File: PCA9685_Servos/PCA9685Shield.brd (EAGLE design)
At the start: 58.2 x 36.2 mm, 13 parts, among them U1 PCA9685

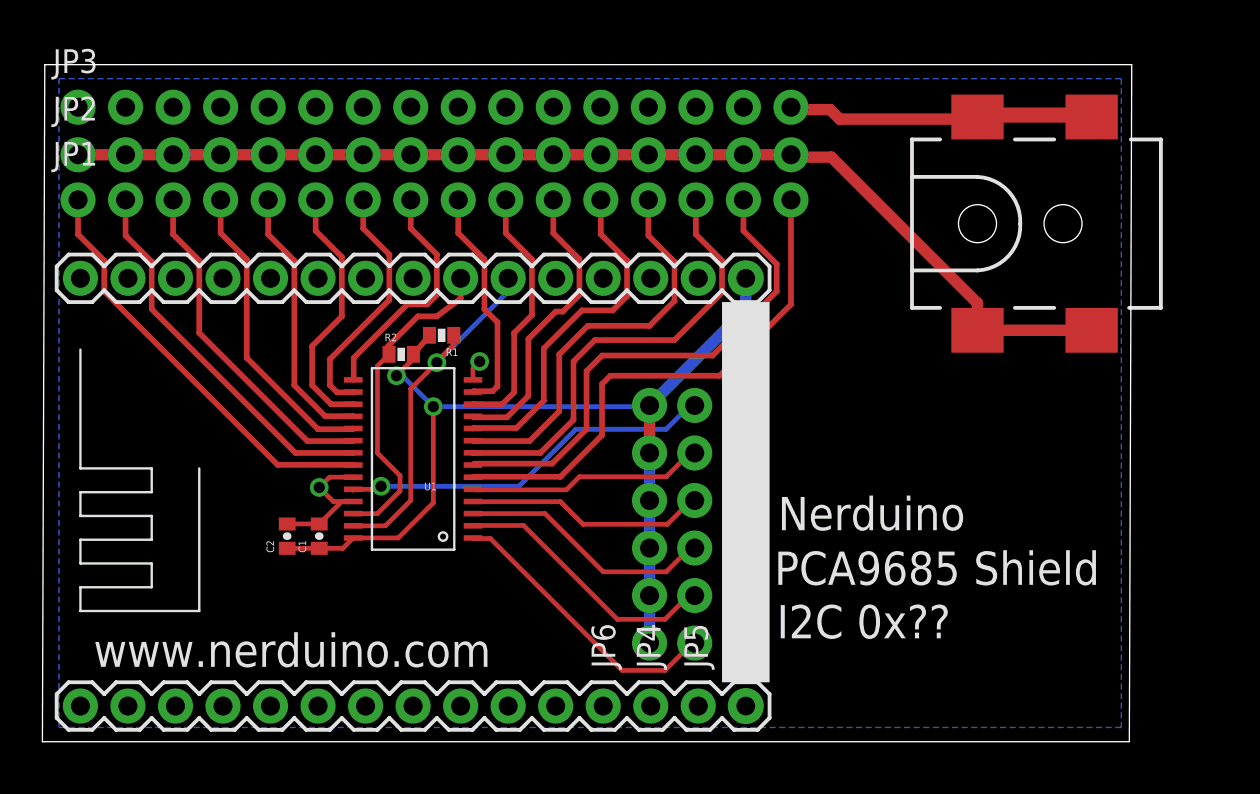
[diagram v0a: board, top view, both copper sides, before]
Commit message: Added solder jumpers for address and added resistors to output pins on pca9685 shield Updated labels
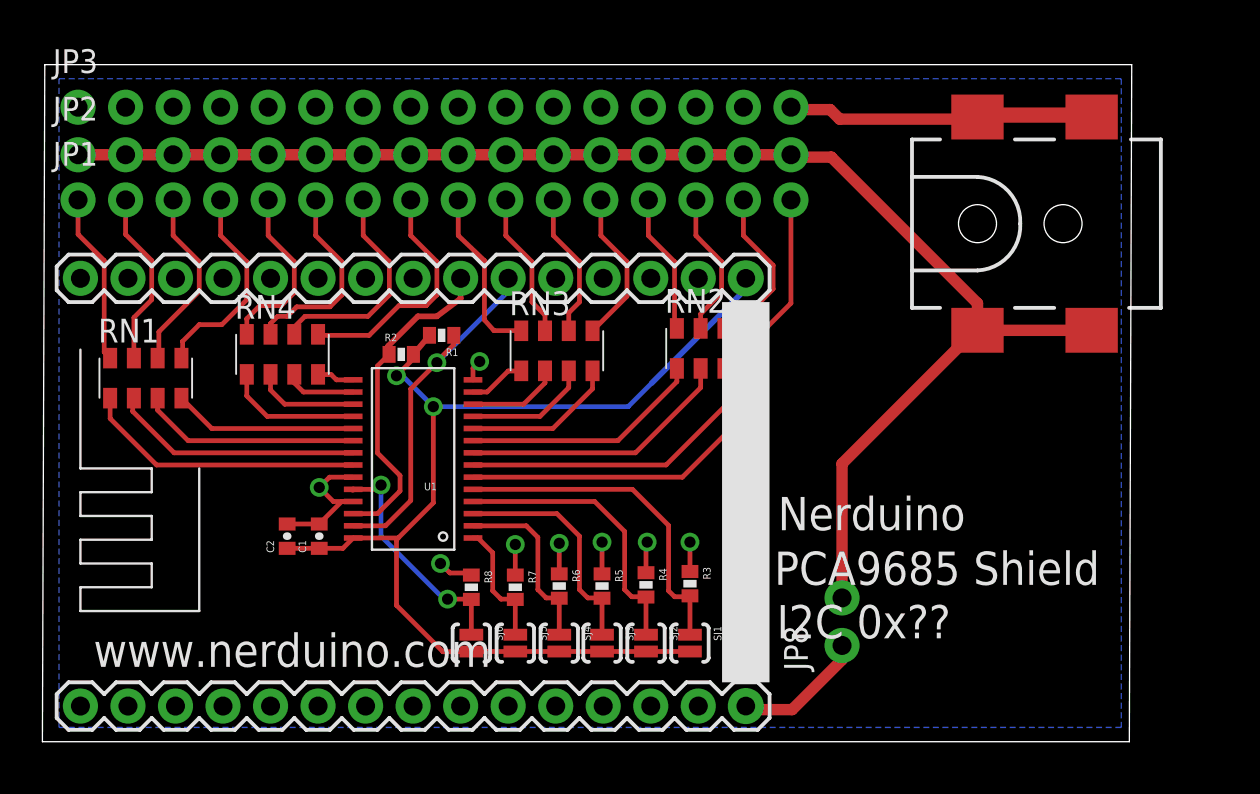
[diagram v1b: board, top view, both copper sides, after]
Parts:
- removed JP4, JP5, JP6: (no value), SparkFun-Connectors:1X06_NO_SILK
- added JP8: (no value), SparkFun:1X02_NO_SILK
- added R3, R4, R5, R6, R7, R8: 10k, SparkFun:0402-RES
- added RN1, RN2, RN3, RN4: 220, resistor-dil:EXBS8V
- added SJ1, SJ2, SJ3, SJ4, SJ5, SJ6: SOLDERJUMPERNO, SparkFun:SJ_2S-NO
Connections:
- removed net N$7: JP4.5, U1.5
- new net N$1: JP8.1, U$1.15
- new net N$27: JP1.2, RN1.7
- new net N$28: JP1.1, RN1.8
- new net N$29: RN1.3, U1.20
- new net N$30: RN1.4, U1.19
- new net N$31: RN4.1, U1.18
- new net N$32: RN4.2, U1.17
- new net N$33: RN4.3, U1.16
- new net N$34: RN4.4, U1.15
- new net N$35: RN3.1, U1.13
- new net N$36: RN3.2, U1.12
- new net N$37: RN3.3, U1.11
- new net N$38: RN3.4, U1.10
- new net N$39: RN2.1, U1.9
- new net N$40: RN2.2, U1.8
- new net N$41: RN2.3, U1.7
- new net N$42: JP1.16, RN2.5
- new net N$43: R3.2, SJ1.1, U1.5
- net 3.3V: now also SJ1.2, SJ2.2, SJ3.2, SJ4.2, SJ5.2, SJ6.2; no longer JP6.1, JP6.2, JP6.3, JP6.4, JP6.5, JP6.6
- net GND: now also R3.1, R4.1, R5.1, R6.1, R7.1, R8.1; no longer JP5.1, JP5.2, JP5.3, JP5.4, JP5.5, JP5.6
- net N$10: now also RN2.4; no longer JP1.16
- net N$11: now also RN2.6; no longer U1.7
- net N$12: now also RN2.7; no longer U1.8
- net N$13: now also RN2.8; no longer U1.9
- net N$14: now also RN3.5; no longer U1.10
- net N$15: now also RN3.6; no longer U1.11
- net N$16: now also RN3.7; no longer U1.12
- net N$17: now also RN3.8; no longer U1.13
- net N$18: now also RN4.5; no longer U1.15
- net N$19: now also RN4.6; no longer U1.16
- net N$20: now also RN4.7; no longer U1.17
- net N$21: now also RN4.8; no longer U1.18
- net N$22: now also RN1.5; no longer U1.19
- net N$23: now also RN1.6; no longer U1.20
- net N$24: now also RN1.2; no longer JP1.2
- net N$25: now also RN1.1; no longer JP1.1
- net N$26: now also JP8.2
- net N$3: now also R7.2, SJ5.1; no longer JP4.1
- net N$4: now also R6.2, SJ4.1; no longer JP4.2
- net N$5: now also R5.2, SJ3.1; no longer JP4.3
- net N$6: now also R4.2, SJ2.1; no longer JP4.4
- net N$9: now also R8.2, SJ6.1; no longer JP4.6
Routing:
- net N$11: track 27.5 -> 9.31 mm
- net N$43: track 0.00 -> 18.1 mm
- net N$26: track 59.1 -> 76.5 mm
- net N$41: track 0.00 -> 16.8 mm
- net N$12: track 24.2 -> 7.88 mm
- net N$40: track 0.00 -> 14.6 mm
- net N$13: track 21.6 -> 7.50 mm
- net N$39: track 0.00 -> 12.9 mm
- net N$7: track 12.7 -> 0.00 mm
- net N$29: track 0.00 -> 11.8 mm
- net GND: track 33.1 -> 44.3 mm, vias 2 -> 8
- net N$14: track 18.5 -> 8.34 mm
- net N$30: track 0.00 -> 9.85 mm
- net N$10: track 28.0 -> 18.5 mm
- net N$27: track 0.00 -> 9.43 mm
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
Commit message: Added OLED Shield Added LiPo Battery Charger Shield Updated outlines of all shields to match the cutout of the nodemcu board
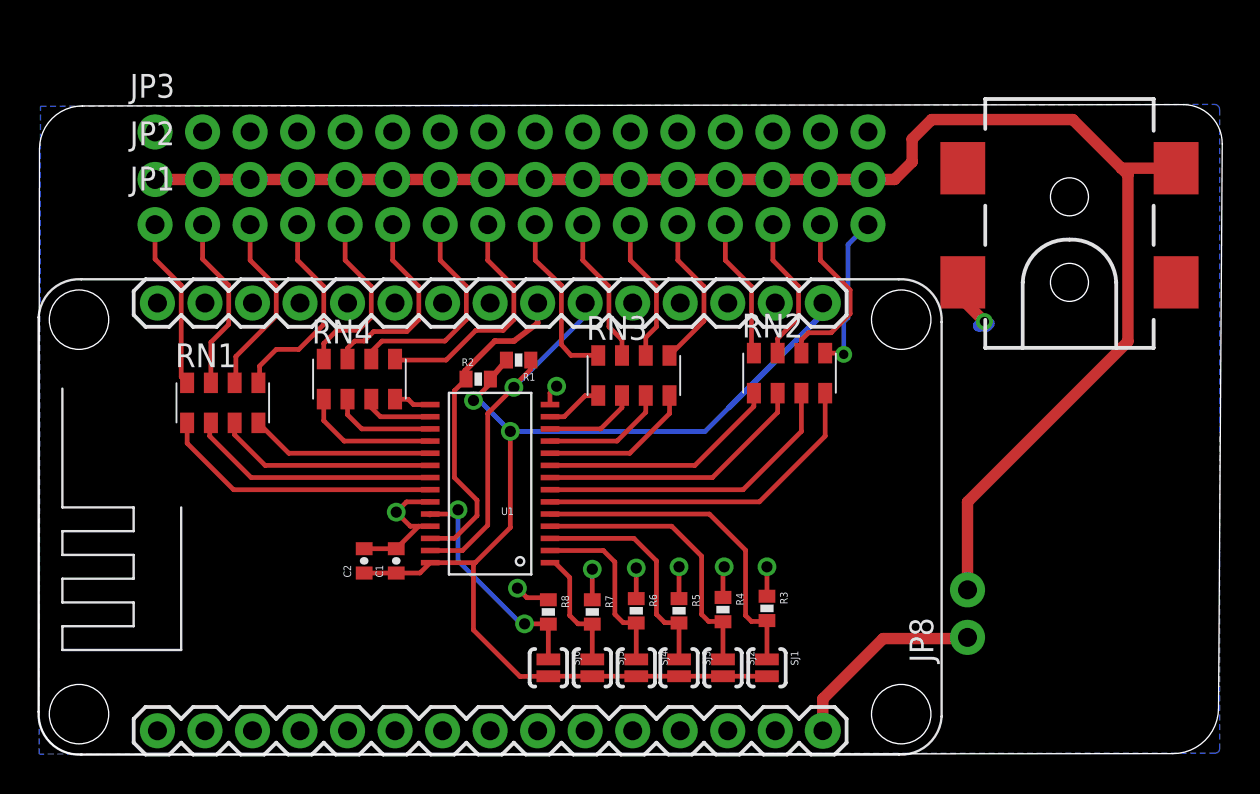
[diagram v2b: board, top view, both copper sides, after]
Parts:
- JP7: value POWER_JACK1 -> POWER_JACKSMD; device SparkFun-Connectors:POWER_JACK_SMD_OVERPASTE_REDBOARD_0603 -> SparkFun:POWER_JACK_SMD
- moved JP8 6.72 mm to (49.9, 6.21)
- moved JP7 5.83 mm to (55.4, 25.2), turned to 90 degrees
- moved R3 4.32 mm to (39.2, 7.76)
- moved R5 4.32 mm to (34.5, 7.63)
- moved R7 4.32 mm to (29.9, 7.57)
- moved SJ1 4.32 mm to (39.2, 4.58)
- moved SJ2 4.32 mm to (36.9, 4.58)
- moved SJ3 4.32 mm to (34.5, 4.58)
- moved SJ5 4.32 mm to (29.9, 4.58)
- moved JP1 4.32 mm to (6.53, 28.3)
- moved R2 4.32 mm to (23.8, 20.0)
- moved R4 4.32 mm to (36.9, 7.70)
- moved C2 4.32 mm to (17.7, 10.3)
- moved JP2 4.32 mm to (6.53, 30.7)
- moved JP3 4.32 mm to (6.53, 33.2)
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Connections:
- net GND: now also U$1.10, U$1.17, U$1.24
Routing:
- net GND: track 44.3 -> 24.0 mm, vias 8 -> 9
- net N$26: track 76.5 -> 83.9 mm
- net N$1: track 7.09 -> 10.8 mm
- net N$42: track 8.37 -> 8.49 mm, vias 0 -> 1
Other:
- board size 58.2 x 36.2 mm -> 63.3 x 34.7 mm
- board text added: "NERDUINO PCA9685 Shield I2C 0x?? www.nerduino.com"
- board text removed: "I2C 0x??"
- board text removed: "Nerduino"
- board text removed: "PCA9685 Shield"
- board text removed: "www.nerduino.com"

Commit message: Updated the i2c pins to all shields to use d11/d12  as these pins will have dual use with the upcoming wifimcu Added FM24W256  Fram shield Added X95840 Digital potentiometer Shield Added AD5696 DAC Shield
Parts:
- SJ1, SJ2, SJ3, SJ4, SJ5, SJ6: value SOLDERJUMPERNO -> (none)
- moved R1 16.9 mm to (19.8, 5.26), turned to 270 degrees
- moved R2 14.9 mm to (21.8, 5.21), turned to 270 degrees
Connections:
- net 3.3V: now also U$1.11
- net GND: no longer U$1.24
- net N$2: now also U$1.5; no longer U$1.21
- net N$8: now also U$1.4; no longer U$1.22
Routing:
- net N$2: track 19.5 -> 13.5 mm, vias 1 -> 0
- net N$8: track 17.4 -> 21.4 mm, vias 0 -> 1
- net 3.3V: track 59.7 -> 57.2 mm, vias 2 -> 3
